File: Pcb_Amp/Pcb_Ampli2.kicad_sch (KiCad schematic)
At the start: 56 parts, among them J1 Conn_01x02, J2 Jack-DC, J3 Jack-DC, J4 Conn_01x02, SW1 SW_SPDT

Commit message: PCBV3_Preamp_Power
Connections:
- net GND: now also R10.1, R5.1, R6.2, R9.2
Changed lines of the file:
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@@
+	)
+	(junction
+		(at 251.46 59.69)
+		(diameter 0)
+		(color 0 0 0 0)
 	)
 	(junction
 		(at 182.88 85.09)
+		(diameter 0)
+		(color 0 0 0 0)
+	)
+	(junction
+		(at 250.19 119.38)
 		(diameter 0)
 		(color 0 0 0 0)
@@
 	(wire
 		(pts
+			(xy 250.19 116.84) (xy 250.19 119.38)
+		)
+		(stroke
+			(width 0)
+			(type default)
+		)
+	)
+	(wire
+		(pts
 			(xy 250.19 102.87) (xy 250.19 104.14)
 		)
@@
 	(wire
 		(pts
-			(xy 250.19 116.84) (xy 250.19 119.38)
-		)
-		(stroke
-			(width 0)
-			(type default)
-		)
-	)
-	(wire
-		(pts
 			(xy 251.46 74.93) (xy 251.46 72.39)
 		)
@@
 	(wire
 		(pts
+			(xy 240.03 119.38) (xy 250.19 119.38)
+		)
+		(stroke
+			(width 0)
+			(type default)
+		)
+	)
+	(wire
+		(pts
 			(xy 133.35 95.25) (xy 115.57 95.25)
 		)
@@
 		)
 		(stroke
+			(width 0)
+			(type default)
+		)
+	)
+	(wire
+		(pts
+			(xy 241.3 59.69) (xy 251.46 59.69)
+		)
+		(stroke

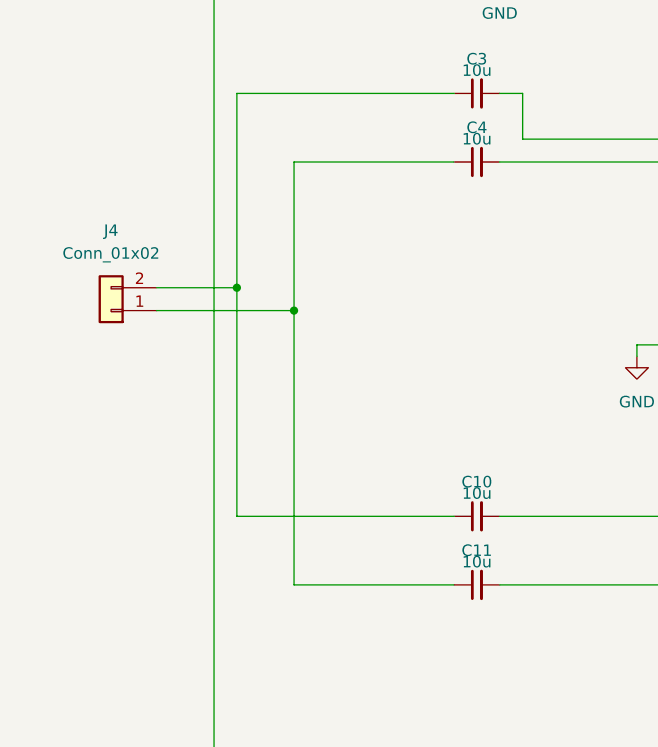
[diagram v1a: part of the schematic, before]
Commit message: PCBV4_Connectors_changed
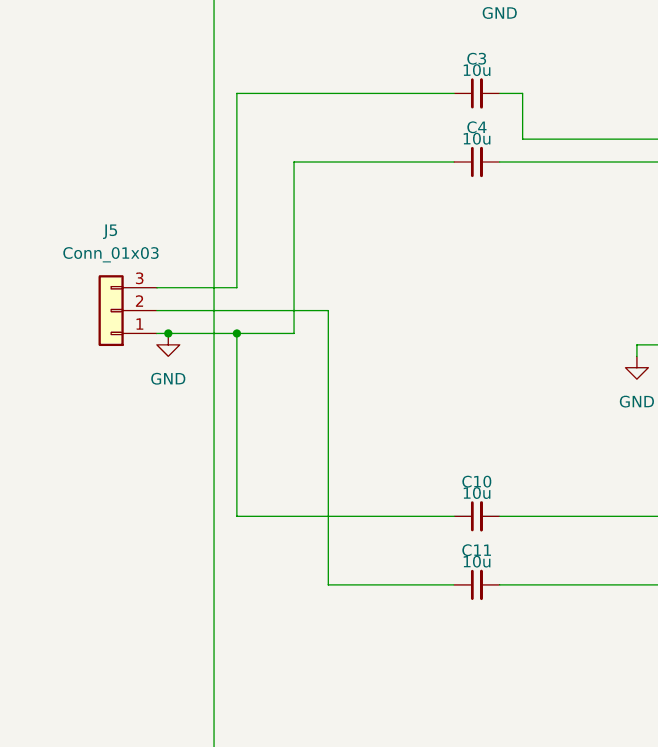
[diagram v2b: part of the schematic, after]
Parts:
- removed J4: Conn_01x02, Connector_AMASS:AMASS_XT60-M_1x02_P7.20mm_Vertical, symbol Connector_Generic:Conn_01x02
- added J5: Conn_01x03, Connector_JST:JST_EH_B3B-EH-A_1x03_P2.50mm_Vertical, symbol Connector_Generic:Conn_01x03
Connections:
- net GND: now also C10.1, C4.1, J5.1 (Pin_1)
- net at C3.1: now also J5.3 (Pin_3); no longer C10.1
- net at C11.1: now also J5.2 (Pin_2); no longer C4.1
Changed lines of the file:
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@@
 	)
 	(junction
+		(at 41.91 91.44)
+		(diameter 0)
+		(color 0 0 0 0)
+	)
+	(junction
 		(at 205.74 82.55)
 		(diameter 0)
@@
 	)
 	(junction
-		(at 41.91 86.36)
-		(diameter 0)
-		(color 0 0 0 0)
-	)
-	(junction
 		(at 210.82 52.07)
 		(diameter 0)
@@
 	)
 	(junction
+		(at 34.29 91.44)
+		(diameter 0)
+		(color 0 0 0 0)
+	)
+	(junction
 		(at 195.58 95.25)
 		(diameter 0)
@@
 	)
 	(junction
-		(at 48.26 88.9)
-		(diameter 0)
-		(color 0 0 0 0)
-	)
-	(junction
 		(at 90.17 67.31)
 		(diameter 0)
@@
 	(wire
 		(pts
+			(xy 34.29 91.44) (xy 41.91 91.44)
+		)
+		(stroke
+			(width 0)
+			(type default)
+		)
+	)
+	(wire
+		(pts
 			(xy 194.31 124.46) (xy 200.66 124.46)
 		)
@@
 	(wire
 		(pts
+			(xy 48.26 91.44) (xy 41.91 91.44)
+		)
+		(stroke
+			(width 0)
+			(type default)
+		)
+	)
+	(wire
+		(pts
 			(xy 179.07 59.69) (xy 187.96 59.69)
 		)
@@
 	(wire
 		(pts
-			(xy 48.26 88.9) (xy 33.02 88.9)
-		)
-		(stroke
-			(width 0)
-			(type default)
-		)
-	)
-	(wire
-		(pts
 			(xy 181.61 77.47) (xy 179.07 77.47)
 		)
@@
 	(wire
 		(pts
-			(xy 48.26 119.38) (xy 48.26 88.9)
-		)
-		(stroke
-			(width 0)
-			(type default)
-		)
-	)
-	(wire
-		(pts
 			(xy 182.88 67.31) (xy 182.88 85.09)
 		)
@@
 	(wire
 		(pts
-			(xy 48.26 72.39) (xy 48.26 88.9)
+			(xy 52.07 48.26) (xy 52.07 49.53)
 		)
 		(stroke
@@
 	(wire
 		(pts
-			(xy 52.07 48.26) (xy 52.07 49.53)
+			(xy 205.74 82.55) (xy 233.68 82.55)
 		)
 		(stroke
@@
 	(wire
 		(pts
-			(xy 205.74 82.55) (xy 233.68 82.55)
+			(xy 133.35 85.09) (xy 100.33 85.09)
 		)
 		(stroke
@@
 	(wire
 		(pts
-			(xy 133.35 85.09) (xy 100.33 85.09)
+			(xy 33.02 91.44) (xy 34.29 91.44)
 		)
 		(stroke
@@
 	(wire
 		(pts
+			(xy 52.07 88.9) (xy 52.07 119.38)
+		)
+		(stroke
+			(width 0)
+			(type default)
+		)
+	)
+	(wire
+		(pts
 			(xy 182.88 87.63) (xy 182.88 105.41)
 		)
@@
 	(wire
 		(pts
+			(xy 41.91 91.44) (xy 41.91 111.76)
+		)
+		(stroke
+			(width 0)
+			(type default)
+		)
+	)
+	(wire
+		(pts
 			(xy 62.23 40.64) (xy 62.23 36.83)
 		)
@@
 	(wire
 		(pts
-			(xy 66.04 119.38) (xy 48.26 119.38)
+			(xy 66.04 119.38) (xy 52.07 119.38)
 		)
 		(stroke
@@
 	(wire
 		(pts
+			(xy 48.26 72.39) (xy 48.26 91.44)
+		)
+		(stroke
+			(width 0)
+			(type default)
+		)
+	)
+	(wire
+		(pts
 			(xy 222.25 111.76) (xy 222.25 113.03)
 		)
@@
 	(wire
 		(pts
+			(xy 33.02 88.9) (xy 52.07 88.9)
+		)
+		(stroke
+			(width 0)
+			(type default)
+		)
+	)
+	(wire
+		(pts
 			(xy 41.91 64.77) (xy 41.91 86.36)
 		)
@@
 	(wire
 		(pts
-			(xy 41.91 111.76) (xy 41.91 86.36)
-		)
-		(stroke
-			(width 0)
-			(type default)
-		)
-	)
-	(wire
-		(pts
 			(xy 205.74 74.93) (xy 205.74 72.39)
 		)
@@
 	)
 	(symbol
+		(lib_name "GND_1")
+		(lib_id "power:GND")
+		(at 34.29 91.44 0)
+		(unit 1)
+		(exclude_from_sim no)
+		(in_bom yes)
+		(on_board yes)
+		(dnp no)
+		(fields_autoplaced yes)
+		(property "Reference" "#PWR013"
+			(at 34.29 97.79 0)
+			(effects
+				(font
+					(size 1.27 1.27)
+				)
+				(hide yes)
+			)
+		)
+		(property "Value" "GND"
+			(at 34.29 96.52 0)
+			(effects
+				(font
+					(size 1.27 1.27)
+				)
+			)
+		)
+		(property "Footprint" ""
+			(at 34.29 91.44 0)
+			(effects
+				(font
+					(size 1.27 1.27)
+				)
+				(hide yes)
+			)
+		)
+		(property "Datasheet" ""
+			(at 34.29 91.44 0)
+			(effects
+				(font
+					(size 1.27 1.27)
+				)
+				(hide yes)
+			)
+		)
+		(property "Description" "Power symbol creates a global label with name \"GND\" , ground"
+			(at 34.29 91.44 0)
+			(effects
+				(font
+					(size 1.27 1.27)
+				)
+				(hide yes)
+			)
+		)
+		(pin "1"
+		)
+		(instances
+			(project ""
+				(path "/64f6da7e-5007-4d1f-8a06-2a947295dae2"
+					(reference "#PWR013")
+					(unit 1)
+				)
+			)
+		)
+	)
+	(symbol
 		(lib_id "Device:C_Small")
 		(at 250.19 106.68 0)
@@
 	)
 	(symbol
+		(lib_id "Connector_Generic:Conn_01x03")
+		(at 27.94 88.9 180)
+		(unit 1)
+		(exclude_from_sim no)
+		(in_bom yes)
+		(on_board yes)
+		(dnp no)
+		(fields_autoplaced yes)
+		(property "Reference" "J5"
+			(at 27.94 80.01 0)
+			(effects
+				(font
+					(size 1.27 1.27)
+				)
+			)
+		)
+		(property "Value" "Conn_01x03"
+			(at 27.94 82.55 0)
+			(effects
+				(font
+					(size 1.27 1.27)
+				)
+			)
+		)
+		(property "Footprint" "Connector_JST:JST_EH_B3B-EH-A_1x03_P2.50mm_Vertical"
+			(at 27.94 88.9 0)
+			(effects
+				(font
+					(size 1.27 1.27)
+				)
+				(hide yes)
+			)
+		)
+		(property "Datasheet" "~"
+			(at 27.94 88.9 0)
+			(effects
+				(font
+					(size 1.27 1.27)
+				)
+				(hide yes)
+			)
+		)
+		(property "Description" "Generic connector, single row, 01x03, script generated (kicad-library-utils/schlib/autogen/connector/)"
+			(at 27.94 88.9 0)
+			(effects
+				(font
+					(size 1.27 1.27)
+				)
+				(hide yes)
+			)
+		)
+		(pin "2"
+		)
+		(pin "1"
+		)
+		(pin "3"
+		)
+		(instances
+			(project ""
+				(path "/64f6da7e-5007-4d1f-8a06-2a947295dae2"
+					(reference "J5")
+					(unit 1)
+				)
+			)
+		)
+	)
+	(symbol
 		(lib_id "power:+24V")
 		(at 50.8 19.05 0)
@@
 					(unit 1)
 				)
-			)
-		)
-	)
-	(symbol
-		(lib_id "Connector_Generic:Conn_01x02")
-		(at 27.94 88.9 180)
-		(unit 1)
-		(exclude_from_sim no)
-		(in_bom yes)
-		(on_board yes)
-		(dnp no)
-		(property "Reference" "J4"
-			(at 27.94 80.01 0)
-			(effects
-				(font
-					(size 1.27 1.27)
-				)
-			)
-		)
-		(property "Value" "Conn_01x02"
-			(at 27.94 82.55 0)
-			(effects
-				(font
-					(size 1.27 1.27)
-				)
-			)
-		)
-		(property "Footprint" "Connector_AMASS:AMASS_XT60-M_1x02_P7.20mm_Vertical"
-			(at 27.94 88.9 0)
-			(effects
-				(font
-					(size 1.27 1.27)
-				)
-				(hide yes)
-			)
-		)
-		(property "Datasheet" "~"
-			(at 27.94 88.9 0)
-			(effects
-				(font
-					(size 1.27 1.27)
-				)
-				(hide yes)
-			)
-		)
-		(property "Description" ""
-			(at 27.94 88.9 0)
-			(effects
-				(font
-					(size 1.27 1.27)
-				)
-			)
-		)
-		(pin "2"
-		)
-		(pin "1"
-		)
-		(instances
-			(project "Pcb_Ampli2"
-				(path "/64f6da7e-5007-4d1f-8a06-2a947295dae2"
-					(reference "J4")
-					(unit 1)
-				)
